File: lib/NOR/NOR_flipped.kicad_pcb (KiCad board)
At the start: 2 copper layers, 4 parts

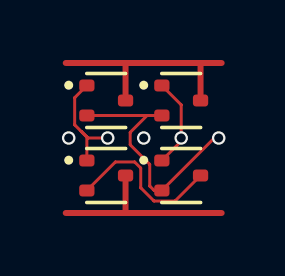
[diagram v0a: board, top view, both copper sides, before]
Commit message: High-density layout with pitch of 1.1mm, which gains 23% !!
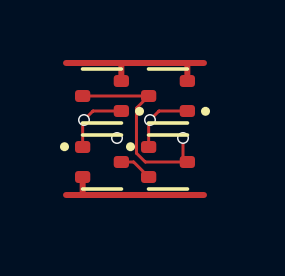
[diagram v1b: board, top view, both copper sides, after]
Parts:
- moved P2 0.63 mm to (3.31, 3.30)
- moved P1 0.47 mm to (1.11, 3.30)
- moved N2 0.46 mm to (3.31, 1.10), turned to 180 degrees
- moved N1 0.21 mm to (1.11, 1.10), turned to 180 degrees
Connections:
- N1 pad 2: Y -> GND
- N1 pad 3: GND -> Y
- N2 pad 2: Y -> GND
- N2 pad 3: GND -> Y
- P1 pad 2: C -> VDD
- P1 pad 3: VDD -> C
- P2 pad 2: Y -> C
- P2 pad 3: C -> Y
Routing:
- net C: track 5.46 -> 1.12 mm
- net Y: track 8.93 -> 6.95 mm
- net GND: track 7.70 -> 5.81 mm
- net A: track 3.81 -> 2.29 mm
- net VDD: track 6.45 -> 5.21 mm
- net B: track 3.03 -> 2.29 mm
- net (no net): vias 2 -> 1
